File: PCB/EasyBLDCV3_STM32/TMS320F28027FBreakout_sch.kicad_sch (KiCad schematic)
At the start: 6 parts

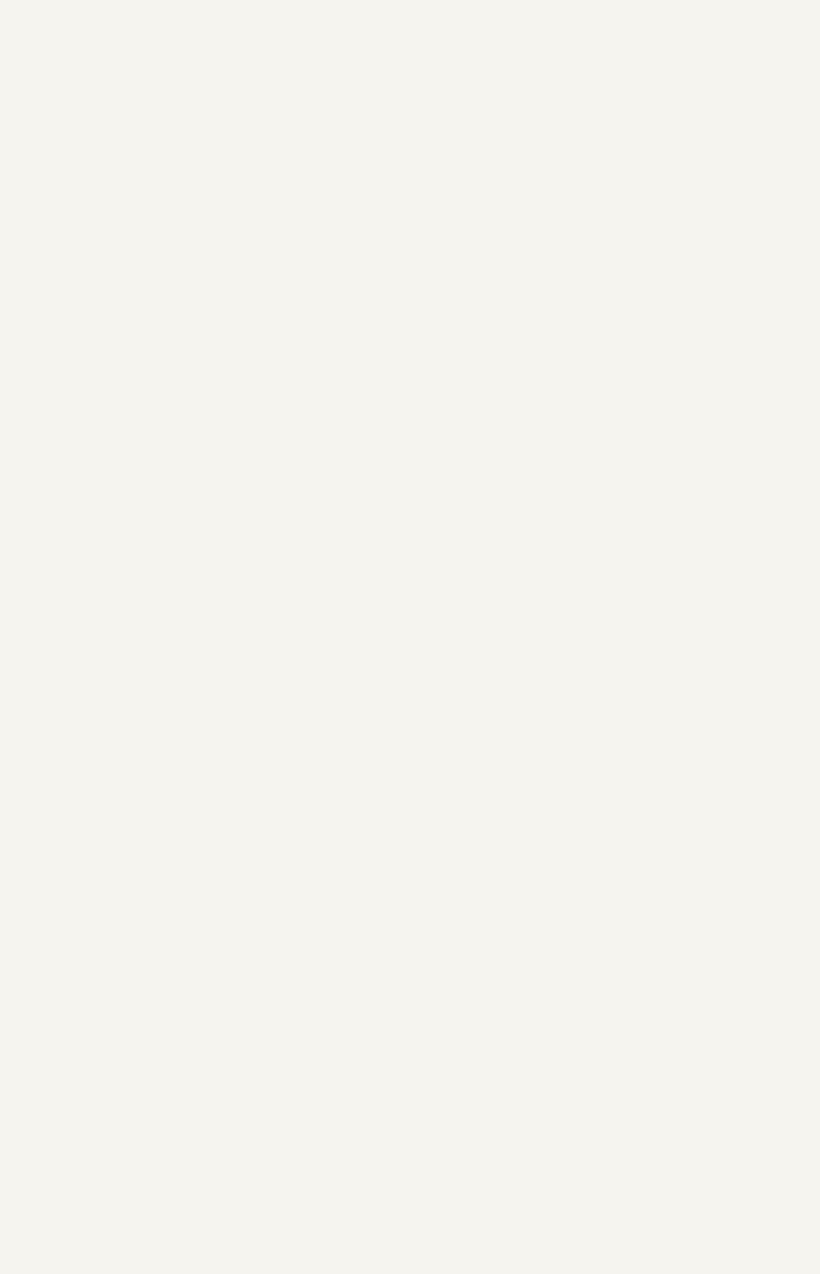
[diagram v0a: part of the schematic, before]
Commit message: Added footprints and began schematic for new gate drive
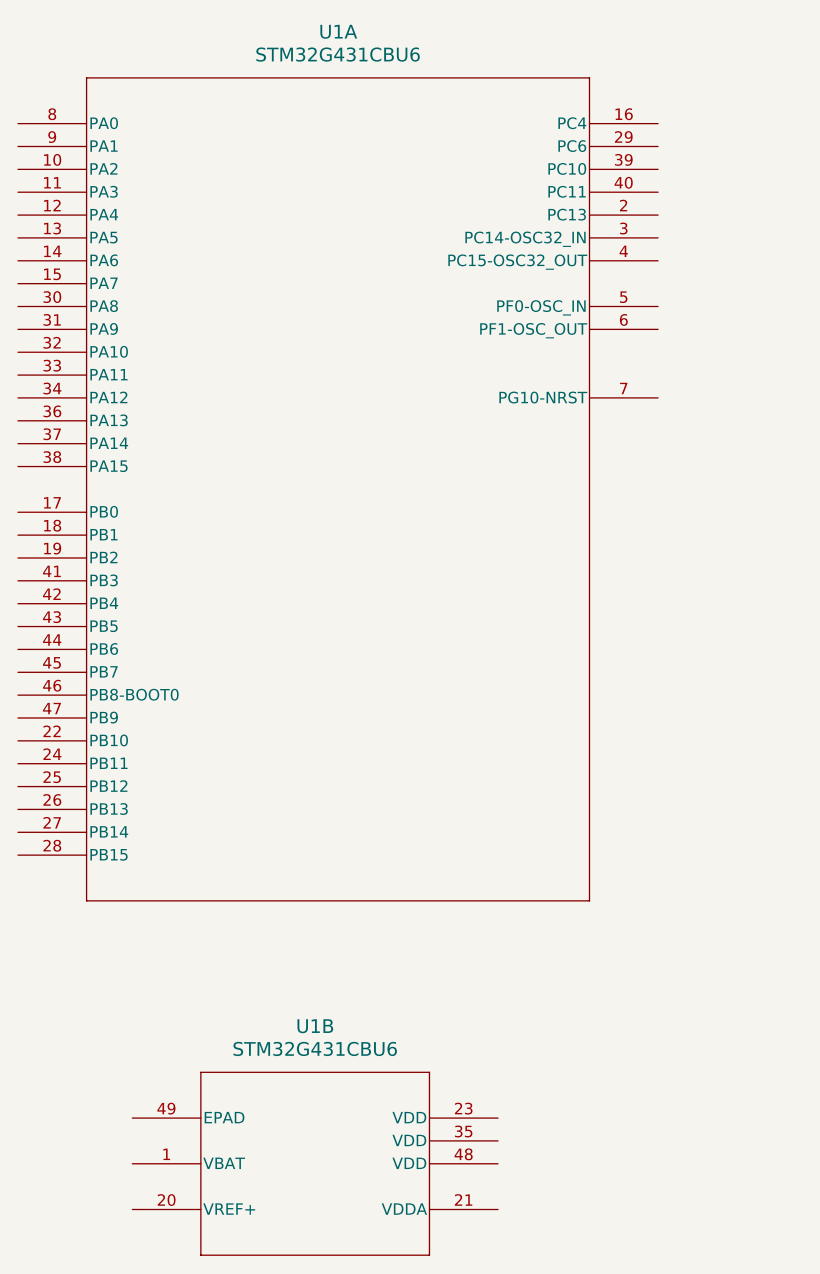
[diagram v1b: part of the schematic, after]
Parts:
- added U1: STM32G431CBU6, UFQFPN-48_7X7X0P55MM, symbol EasyBLDC:STM32G431CBU6
